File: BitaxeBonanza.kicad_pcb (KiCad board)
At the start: 6 copper layers, 130 x 112 mm, 317 parts, among them J1 XT30, J2 TC2030-IDC, J3 Conn_01x04, J4 Conn_01x08, J5 USB_C_Receptacle_USB2.0, J7 Conn_01x04, J8 Conn_01x04, SW1 SWITCH-SPST, SW2 SWITCH-SPST, U1 TPSM861253RDXR, U10 MCP1824T-1202E/OT, U11 MCP1824T-1202E/OT, U13 EMC2302, U2 L78L05_SOT89, U3 TPS546D24ARVFR, U4 TPS546D24ARVFR, U5 ESP32-S3-WROOM-1, U6 25MHz, U7 SN74AVC4T774, U8 MCP1824T-1202E/OT, U9 MCP1824T-1202E/OT

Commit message: ASICs placed. most other parts placed.
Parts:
- removed C100, C106, C107, C113, C114, C120, C121, C127, C128, C134, C135, C141, C142, C148, C149, C155, C156, C162, C163, C169, C170, C176, C177, C71, C72, C78, C79, C85, C86, C92, C93, C99: 10uF, Capacitor_SMD:C_0603_1608Metric
- removed C103, C104, C105, C110, C111, C112, C117, C118, C119, C124, C125, C126, C131, C132, C133, C138, C139, C140, C145, C146, C147, C152, C153, C154, C159, C160, C161, C166, C167, C168, C173, C174, C175, C68, C69, C70, C75, C76, C77, C82, C83, C84, C89, C90, C91, C96, C97, C98: 0.1uF, Capacitor_SMD:C_0402_1005Metric
- removed H10, H11, H12, H5, H6, H7, H8, H9: MountingHole_Pad, bitaxe:Sinhoo SMTSO3015CTJ_nopaste
- removed R12, R13, R16: R, Resistor_SMD:R_0402_1005Metric
- removed R20, R22: 0, Resistor_SMD:R_0402_1005Metric
- removed TP25, TP26, TP27, TP28: TestPoint, TestPoint:TestPoint_Pad_D1.0mm
- added C188: 100uF, Capacitor_SMD:C_1206_3216Metric, B.Cu at (116.1, 114.7)
- added C189: 100uF, Capacitor_SMD:C_1206_3216Metric, B.Cu at (116.2, 109.2)
- added C190: 100uF, Capacitor_SMD:C_1206_3216Metric, B.Cu at (145.6, 114.6)
- added C191: 100uF, Capacitor_SMD:C_1206_3216Metric, B.Cu at (134.3, 114.8)
- added C192: 100uF, Capacitor_SMD:C_1206_3216Metric, B.Cu at (145.5, 104.6)
- added C193: 100uF, Capacitor_SMD:C_1206_3216Metric, B.Cu at (141.8, 100.2)
- added C194: 100uF, Capacitor_SMD:C_1206_3216Metric, B.Cu at (181.3, 119.5)
- added C195: 100uF, Capacitor_SMD:C_1206_3216Metric, B.Cu at (187.2, 110.5)
- added C196: 100uF, Capacitor_SMD:C_1206_3216Metric, B.Cu at (181.3, 104.7)
- added C197: 100uF, Capacitor_SMD:C_1206_3216Metric, B.Cu at (209.5, 104.6)
- added C198: 100uF, Capacitor_SMD:C_1206_3216Metric, B.Cu at (201.1, 105.6)
- added C199: 100uF, Capacitor_SMD:C_1206_3216Metric, B.Cu at (209.6, 114.4)
- added C200: 100uF, Capacitor_SMD:C_1206_3216Metric, B.Cu at (198.6, 114.6)
- added C65: 10uF, Capacitor_SMD:C_0603_1608Metric, B.Cu at (137.4, 143.7)
- added C66: 10uF, Capacitor_SMD:C_0603_1608Metric, B.Cu at (203.4, 143.6)
- added C67: 0.1uF, Capacitor_SMD:C_0402_1005Metric, B.Cu at (137.4, 145.5)
- added H15: ~, bitaxe:bitaxeGT_extruded_heatsink, F.Cu at (106.0, 137.0)
- added H16: ~, bitaxe:bitaxeGT_extruded_heatsink, F.Cu at (171.0, 137.0)
- added R29: 10k, Resistor_SMD:R_0402_1005Metric, B.Cu at (137.4, 147.2)
- added R30: 10k, Resistor_SMD:R_0402_1005Metric, B.Cu at (203.8, 147.8)
- C101, C102, C108, C109, C115, C116, C122, C123, C129, C130, C136, C137, C143, C144, C150, C151, C157, C158, C164, C165, C171, C172, C178, C179, C49, C50, C51, C52, C53, C54, C55, C56, C57, C58, C59, C60, C61, C62, C63, C64, C73, C74, C80, C81, C87, C88, C94, C95, R51, R52, TP15, TP16, TP17, TP18, TP19, TP20, TP21, TP22, TP6, U10, U11, U13, U8, U9: moved to B.Cu
- C183: value 311-3342-1-ND -> 0.1uF; moved to B.Cu
- C184: value 220uF -> 0.1uF; footprint Capacitor_SMD:CP_Elec_6.3x7.7 -> Capacitor_SMD:C_0402_1005Metric; moved to B.Cu
- C185: value 220uF -> 100uF; footprint Capacitor_SMD:CP_Elec_6.3x7.7 -> Capacitor_SMD:C_1206_3216Metric; moved to B.Cu
- C186, C187: value 311-3342-1-ND -> 100uF; footprint Capacitor_SMD:C_0402_1005Metric -> Capacitor_SMD:C_1206_3216Metric; moved to B.Cu
- moved TP22 188.3 mm to (139.1, 129.6)
- moved C73 188.1 mm to (193.9, 117.0)
- moved C74 185.2 mm to (193.9, 114.6)
- moved C171 180.8 mm to (209.6, 119.2)
- moved TP19 179.0 mm to (209.3, 128.3)
- moved C172 178.5 mm to (209.6, 116.8)
- moved C178 176.9 mm to (198.6, 119.4)
- moved C179 174.1 mm to (198.6, 117.0)
- moved C157 172.6 mm to (209.5, 109.4)
- moved C158 171.0 mm to (209.5, 107.0)
- moved C143 168.0 mm to (187.2, 108.1)
- moved C144 165.0 mm to (187.2, 105.7)
- moved C164 161.3 mm to (201.1, 110.4)
- moved C57 159.0 mm to (206.1, 131.3)
- moved C165 158.1 mm to (201.1, 108.0)
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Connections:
- A1 pad 30: unconnected-(A1-VDDIO-Pad30) -> /ASIC/1V2
- A2 pad 19: /ASIC/1V2 -> unconnected-(A2-VDDIO-Pad19)
- A3 pad 19: /ASIC/1V2-1 -> unconnected-(A3-VDDIO-Pad19)
- A4 pad 30: unconnected-(A4-VDDIO-Pad30) -> /ASIC/1V2-1
- A5 pad 30: unconnected-(A5-VDDIO-Pad30) -> /ASIC/1V2-2
- A6 pad 19: /ASIC/1V2-2 -> unconnected-(A6-VDDIO-Pad19)
- A7 pad 19: /ASIC/1V2-3 -> unconnected-(A7-VDDIO-Pad19)
- A8 pad 30: unconnected-(A8-VDDIO-Pad30) -> /ASIC/1V2-3
- C185 pad 1: /5V -> /ASIC/bypass5-1/out
- C185 pad 2: GND -> /ASIC/GND3
- C186 pad 1: /5V -> /ASIC/bypass1-1/out
- C186 pad 2: GND -> /ASIC/GND1
- C187 pad 1: /5V -> /ASIC/bypass2-1/out
- C187 pad 2: GND -> /ASIC/GND1
- C27 pad 1: Net-(C27-Pad1) -> Net-(U3-BOOT)
- C28 pad 1: Net-(C28-Pad1) -> Net-(U4-BOOT)
- J7 pad 2: /5V -> /12V
- J8 pad 2: /5V -> /12V
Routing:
- net /Power/BP1v5_2: track 61.0 -> 14.0 mm, vias 2 -> 1
- net /Power/BCX_DAT: track 71.9 -> 27.0 mm
- net /5V: track 156.2 -> 121.1 mm, vias 5 -> 4
- net /3V3: track 119.9 -> 86.2 mm
- net /Vcore: track 74.9 -> 42.8 mm, vias 104 -> 126
- net /ASIC/shifter4-5/RX_IN: track 0.00 -> 30.9 mm, vias 0 -> 1
- net /ASIC/shifter4-5/TX_OUT: track 0.00 -> 28.7 mm, vias 0 -> 1
- net /ASIC/shifter4-5/RESET_OUT: track 0.00 -> 27.8 mm, vias 0 -> 1
- net /Power/ALRT_VR: track 54.5 -> 26.7 mm, vias 4 -> 2
- net /ASIC/shifter4-5/RESET_IN: track 0.00 -> 26.9 mm, vias 0 -> 1
- net /ASIC/shifter4-5/RX_OUT: track 0.00 -> 26.7 mm, vias 0 -> 1
- net /ASIC/shifter4-5/TRIP_OUT: track 0.00 -> 25.8 mm, vias 0 -> 1
- net /ASIC/shifter4-5/TRIP_IN: track 0.00 -> 25.7 mm, vias 0 -> 1
- net /ASIC/1V2-2: track 0.00 -> 24.9 mm, vias 0 -> 4
- net /ASIC/shifter4-5/TX_IN: track 0.00 -> 24.0 mm, vias 0 -> 1
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- added copper zone on In2.Cu, net /ASIC/GND1
- added copper zone on In3.Cu, net /ASIC/GND1
- added copper zone on In4.Cu, net /ASIC/GND1
- added copper zone on In2.Cu, net /ASIC/GND2
- added copper zone on In3.Cu, net /ASIC/GND2
- added copper zone on In4.Cu, net /ASIC/GND2
- added copper zone on In2.Cu, net /ASIC/GND3
- added copper zone on In3.Cu, net /ASIC/GND3
- added copper zone on In4.Cu, net /ASIC/GND3
- added copper zone on In3.Cu, net /Vcore
- added copper zone on In4.Cu, net /Vcore
- removed copper zone on In2.Cu, net /Power/AGND2
- removed copper zone on In4.Cu, net GND

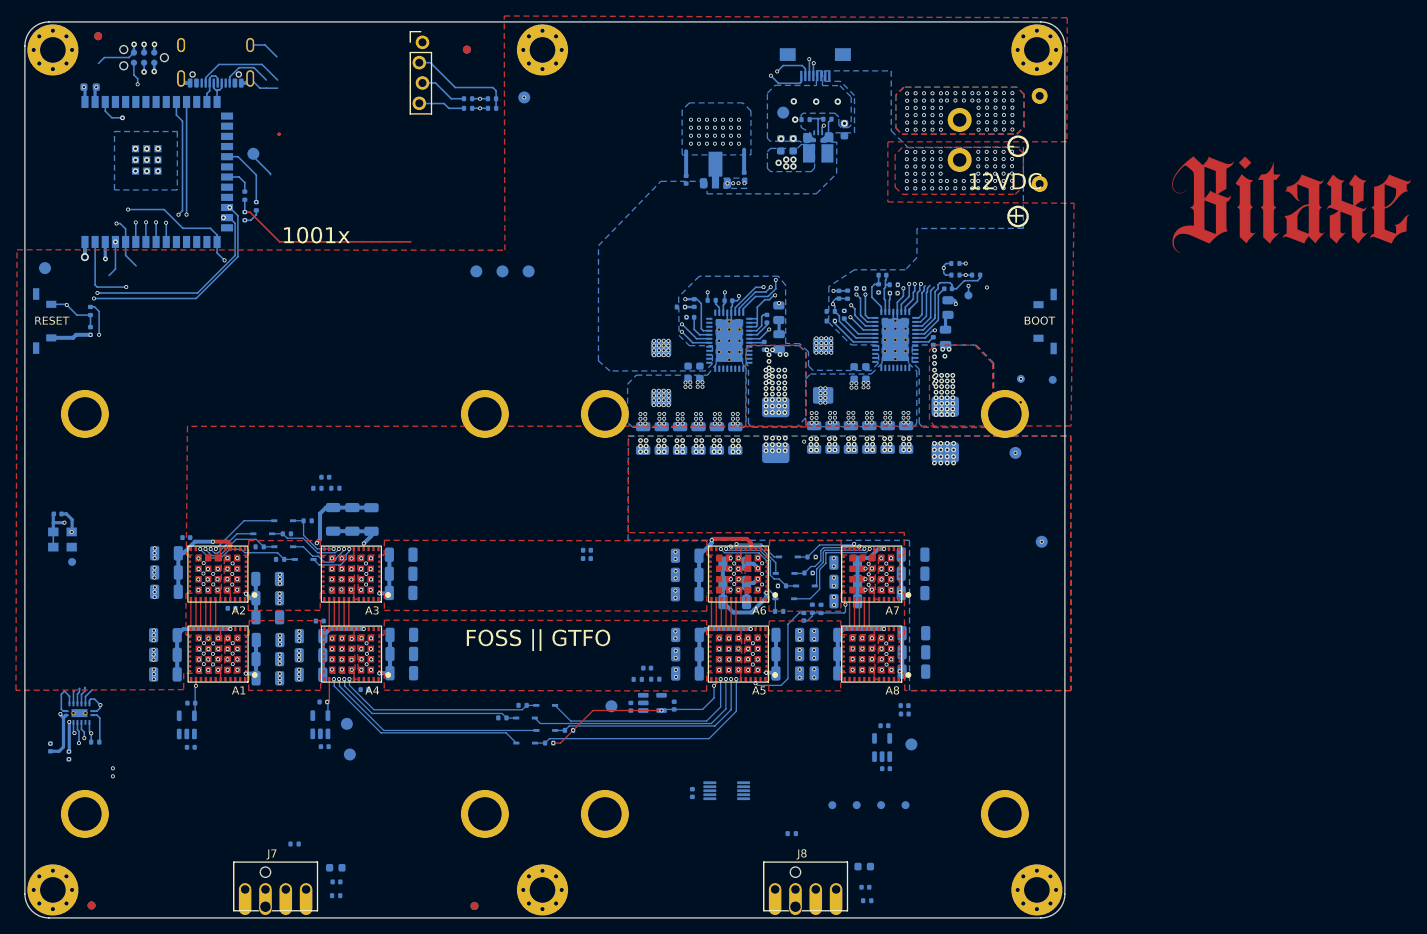
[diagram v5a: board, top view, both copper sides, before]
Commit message: routing is done. Power planes look good. DRC pass
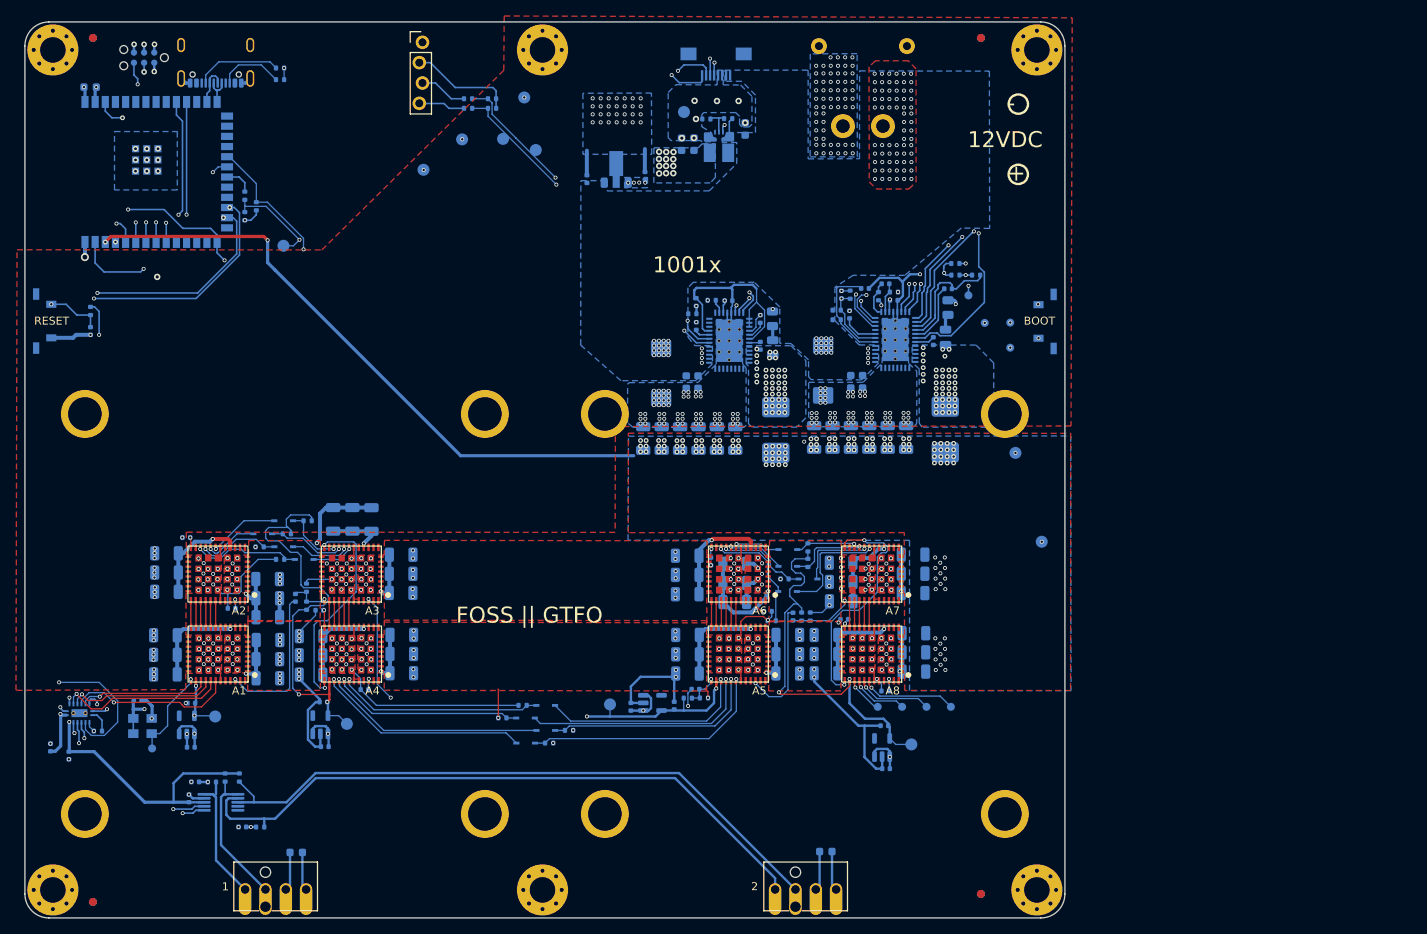
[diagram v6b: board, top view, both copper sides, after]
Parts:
- removed the G*** at (256.3, 61.2)
- added FID5: Fiducial, bitaxe:Fiducial_1mm_Mask2mm, B.Cu at (218.0, 147.0)
- added FID6: Fiducial, bitaxe:Fiducial_1mm_Mask2mm, B.Cu at (107.0, 148.0)
- added FID7: Fiducial, bitaxe:Fiducial_1mm_Mask2mm, B.Cu at (218.0, 40.0)
- added FID8: Fiducial, bitaxe:Fiducial_1mm_Mask2mm, B.Cu at (107.0, 40.0)
- added R20: 5.1k, Resistor_SMD:R_0402_1005Metric, B.Cu at (130.4, 43.8)
- added R22: 5.1k, Resistor_SMD:R_0402_1005Metric, B.Cu at (130.4, 45.2)
- moved G*** 94.0 mm to (162.2, 65.7)
- moved C184 78.2 mm to (125.7, 138.6), turned to 180 degrees
- moved R30 76.4 mm to (127.9, 138.6), turned to 180 degrees
- moved R52 69.4 mm to (125.3, 132.4), turned to 90 degrees
- moved FID4 64.3 mm to (218.0, 40.0)
- moved FID3 63.3 mm to (218.0, 147.0)
- moved U13 63.2 mm to (123.0, 135.5)
- moved C183 62.9 mm to (119.0, 135.1)
- moved TP6 54.6 mm to (153.2, 52.7)
- moved C46 25.4 mm to (112.6, 122.8)
- moved TP14 25.4 mm to (114.4, 128.8)
- moved U6 25.4 mm to (113.2, 126.0)
- moved TP2 24.3 mm to (130.8, 66.0)
- moved C53 23.6 mm to (191.4, 111.7)
- moved C67 21.6 mm to (119.8, 133.0), turned to 180 degrees
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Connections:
- C46 pad 1: /ASIC/1V5 -> /ASIC/1V2
- J4 pad 1: /ESP32/12V -> /12V
- J4 pad 2: /ESP32/12V -> /12V
- J5 pad A5: unconnected-(J5-CC1-PadA5) -> Net-(J5-CC1)
- J5 pad B5: unconnected-(J5-CC2-PadB5) -> Net-(J5-CC2)
- U6 pad 1: /ASIC/1V5 -> /ASIC/1V2
- U6 pad 4: /ASIC/1V5 -> /ASIC/1V2
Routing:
- net /5V: track 121.1 -> 270.4 mm, vias 4 -> 11
- net /12V: track 104.5 -> 203.0 mm, vias 100 -> 108
- net /ASIC/TRIP_3V3: track 0.00 -> 91.7 mm, vias 0 -> 2
- net /Power/ALRT_VR: track 26.7 -> 117.2 mm
- net /fan/FAN2_PWM: track 0.00 -> 81.9 mm
- net /fan/FAN2_TACH: track 0.00 -> 80.5 mm
- net /ESP32/IO0: track 82.5 -> 149.9 mm, vias 3 -> 4
- net /Power/PGOOD: track 42.0 -> 108.4 mm, vias 1 -> 2
- net /Vcore: track 42.8 -> 100.6 mm, vias 126 -> 153
- net /ASIC/REFCLKOUT2: track 0.00 -> 53.4 mm, vias 0 -> 3
- net Net-(J4-Pin_8): track 34.8 -> 87.5 mm
- net Net-(J4-Pin_7): track 34.8 -> 87.5 mm
- net Net-(J4-Pin_6): track 35.4 -> 86.4 mm
- net Net-(J4-Pin_5): track 34.3 -> 83.7 mm
- net /ASIC/1V2-3: track 0.02 -> 48.8 mm
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- added copper zone on In4.Cu, net /12V
- added copper zone on In3.Cu, net /Power/SW1
- added copper zone on In4.Cu, net /Power/SW1
- added copper zone on In3.Cu, net /Power/SW2
- added copper zone on In4.Cu, net /Power/SW2
- added copper zone on In4.Cu, net GND
- removed copper zone on In2.Cu, net /Power/AGND1
- removed copper zone on F.Cu, net /Power/SW1
- removed copper zone on F.Cu, net /Power/SW2
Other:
- board text added: "1"
- board text added: "2"
